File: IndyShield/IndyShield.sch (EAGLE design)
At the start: 18 parts, among them U1 ARDUINOR3-BPLACE

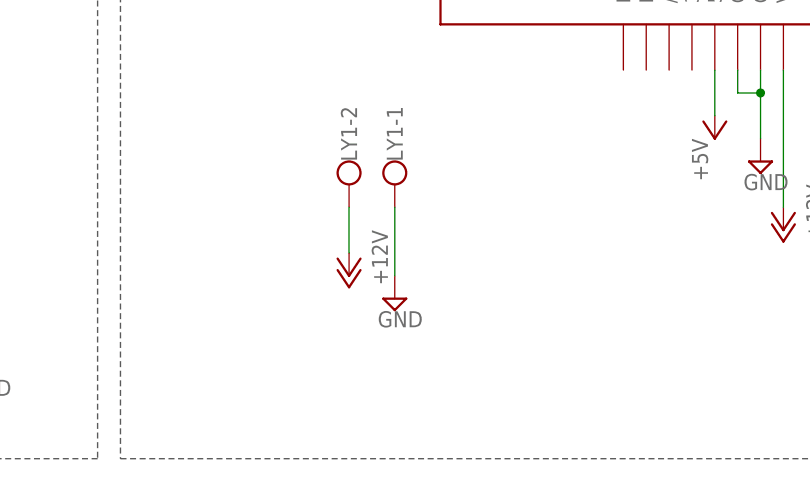
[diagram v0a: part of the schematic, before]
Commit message: Updated IndyShield to V2
Swapped Z axis limit with spindle enable as it should be for current version of GRBL
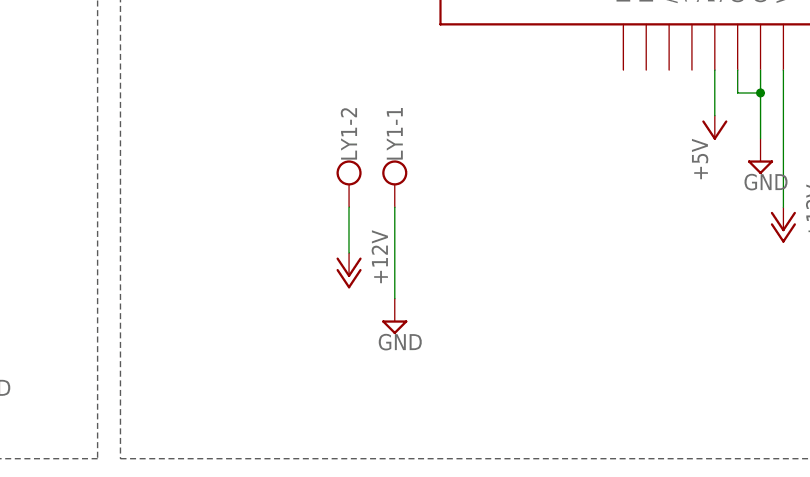
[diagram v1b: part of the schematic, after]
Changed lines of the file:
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@@
 <attribute name="NAME" x="92.329" y="38.1" size="1.778" layer="95" rot="R90"/>
 </instance>
-<instance part="SUPPLY10" gate="GND" x="96.52" y="22.86" smashed="yes">
-<attribute name="VALUE" x="94.615" y="19.685" size="1.778" layer="96"/>
+<instance part="SUPPLY10" gate="GND" x="96.52" y="20.32" smashed="yes">
+<attribute name="VALUE" x="94.615" y="17.145" size="1.778" layer="96"/>
 </instance>
 <instance part="P+3" gate="1" x="91.44" y="25.4" smashed="yes" rot="R180">
@@
 <pinref part="LY1" gate="-1" pin="KL"/>
 <pinref part="SUPPLY10" gate="GND" pin="GND"/>
-<wire x1="96.52" y1="33.02" x2="96.52" y2="25.4" width="0.1524" layer="91"/>
+<wire x1="96.52" y1="33.02" x2="96.52" y2="22.86" width="0.1524" layer="91"/>
 </segment>
 <segment>
